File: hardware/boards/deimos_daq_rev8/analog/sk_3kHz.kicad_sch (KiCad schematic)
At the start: 9 parts, among them Q33001 MMBFJ113, Q33002 MMBFJ113, U33001 OPA196xDBV

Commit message: finish routing new encoder channels. spread nc channels on connectors and update enclosure graphics. only support 2-wire 4-20mA to protect ground.
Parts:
- renumbered C33001 to C45001, C33002 to C45002, C33003 to C45003, C33004 to C45004, Q33001 to Q45001, Q33002 to Q45002, R33001 to R45001, R33002 to R45002, U33001 to U45001
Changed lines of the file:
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@@
 		(on_board yes)
 		(dnp no)
-		(property "Reference" "#PWR286"
+		(property "Reference" "#PWR351"
 			(at 113.03 88.9 0)
 			(effects
@@
 		(on_board yes)
 		(dnp no)
-		(property "Reference" "C33001"
+		(property "Reference" "C45001"
 			(at 106.68 96.012 90)
 			(effects
@@
 		(on_board yes)
 		(dnp no)
-		(property "Reference" "#PWR283"
+		(property "Reference" "#PWR349"
 			(at 92.964 110.49 0)
 			(effects
@@
 		(on_board yes)
 		(dnp no)
-		(property "Reference" "R33001"
+		(property "Reference" "R45001"
 			(at 82.55 77.343 90)
 			(effects
@@
 		(on_board yes)
 		(dnp no)
-		(property "Reference" "#PWR278"
+		(property "Reference" "#PWR346"
 			(at 124.46 92.71 0)
 			(effects
@@
 		(on_board yes)
 		(dnp no)
-		(property "Reference" "Q33001"
+		(property "Reference" "Q45001"
 			(at 80.772 100.584 90)
 			(effects
@@
 		(on_board yes)
 		(dnp no)
-		(property "Reference" "#PWR280"
+		(property "Reference" "#PWR347"
 			(at 124.46 77.47 0)
 			(effects
@@
 		(on_board yes)
 		(dnp no)
-		(property "Reference" "Q33002"
+		(property "Reference" "Q45002"
 			(at 92.964 91.44 90)
 			(effects
@@
 		(on_board yes)
 		(dnp no)
-		(property "Reference" "U33001"
+		(property "Reference" "U45001"
 			(at 107.442 78.994 0)
 			(effects
@@
 		(on_board yes)
 		(dnp no)
-		(property "Reference" "R33002"
+		(property "Reference" "R45002"
 			(at 93.98 77.343 90)
 			(effects
@@
 		(on_board yes)
 		(dnp no)
-		(property "Reference" "C33003"
+		(property "Reference" "C45003"
 			(at 119.38 81.788 90)
 			(effects
@@
 		(on_board yes)
 		(dnp no)
-		(property "Reference" "C33004"
+		(property "Reference" "C45004"
 			(at 118.872 97.536 90)
 			(effects
@@
 		(on_board yes)
 		(dnp no)
-		(property "Reference" "C33002"
+		(property "Reference" "C45002"
 			(at 111.252 65.532 90)
 			(effects
@@
 		(on_board yes)
 		(dnp no)
-		(property "Reference" "#PWR281"
+		(property "Reference" "#PWR348"
 			(at 113.03 81.28 0)
 			(effects
@@
 		(on_board yes)
 		(dnp no)
-		(property "Reference" "#PWR200"
+		(property "Reference" "#PWR250"
 			(at 101.6 99.06 0)
 			(effects

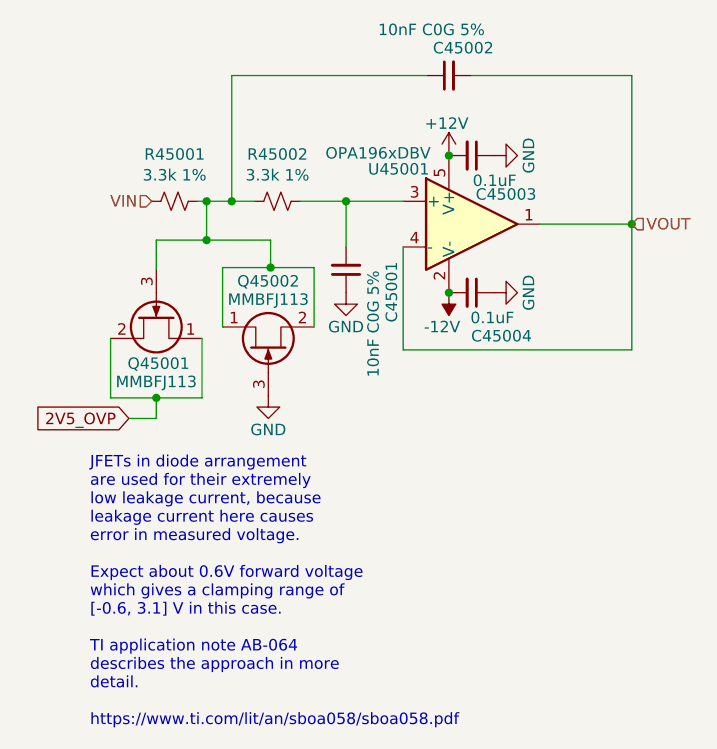
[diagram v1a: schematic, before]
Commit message: finish layout and generate fab files
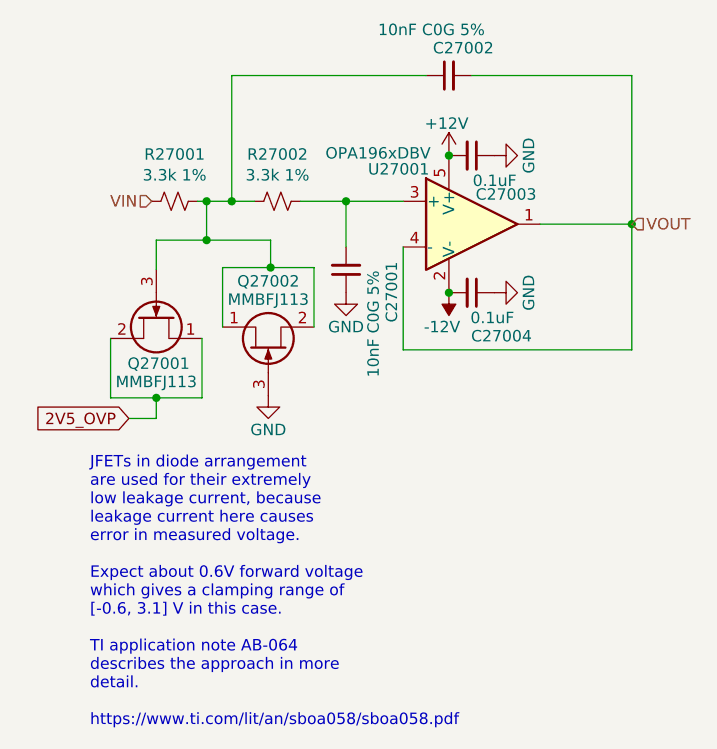
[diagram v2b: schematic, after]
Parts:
- renumbered C45001 to C27001, C45002 to C27002, C45003 to C27003, C45004 to C27004, Q45001 to Q27001, Q45002 to Q27002, R45001 to R27001, R45002 to R27002, U45001 to U27001
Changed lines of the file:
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@@
 		(on_board yes)
 		(dnp no)
-		(property "Reference" "#PWR351"
+		(property "Reference" "#PWR246"
 			(at 113.03 88.9 0)
 			(effects
@@
 		(on_board yes)
 		(dnp no)
-		(property "Reference" "C45001"
+		(property "Reference" "C27001"
 			(at 106.68 96.012 90)
 			(effects
@@
 		(on_board yes)
 		(dnp no)
-		(property "Reference" "#PWR349"
+		(property "Reference" "#PWR244"
 			(at 92.964 110.49 0)
 			(effects
@@
 		(on_board yes)
 		(dnp no)
-		(property "Reference" "R45001"
+		(property "Reference" "R27001"
 			(at 82.55 77.343 90)
 			(effects
@@
 		(on_board yes)
 		(dnp no)
-		(property "Reference" "#PWR346"
+		(property "Reference" "#PWR239"
 			(at 124.46 92.71 0)
 			(effects
@@
 		(on_board yes)
 		(dnp no)
-		(property "Reference" "Q45001"
+		(property "Reference" "Q27001"
 			(at 80.772 100.584 90)
 			(effects
@@
 		(on_board yes)
 		(dnp no)
-		(property "Reference" "#PWR347"
+		(property "Reference" "#PWR242"
 			(at 124.46 77.47 0)
 			(effects
@@
 		(on_board yes)
 		(dnp no)
-		(property "Reference" "Q45002"
+		(property "Reference" "Q27002"
 			(at 92.964 91.44 90)
 			(effects
@@
 		(on_board yes)
 		(dnp no)
-		(property "Reference" "U45001"
+		(property "Reference" "U27001"
 			(at 107.442 78.994 0)
 			(effects
@@
 		(on_board yes)
 		(dnp no)
-		(property "Reference" "R45002"
+		(property "Reference" "R27002"
 			(at 93.98 77.343 90)
 			(effects
@@
 		(on_board yes)
 		(dnp no)
-		(property "Reference" "C45003"
+		(property "Reference" "C27003"
 			(at 119.38 81.788 90)
 			(effects
@@
 		(on_board yes)
 		(dnp no)
-		(property "Reference" "C45004"
+		(property "Reference" "C27004"
 			(at 118.872 97.536 90)
 			(effects
@@
 		(on_board yes)
 		(dnp no)
-		(property "Reference" "C45002"
+		(property "Reference" "C27002"
 			(at 111.252 65.532 90)
 			(effects
@@
 		(on_board yes)
 		(dnp no)
-		(property "Reference" "#PWR348"
+		(property "Reference" "#PWR243"
 			(at 113.03 81.28 0)
 			(effects
@@
 		(on_board yes)
 		(dnp no)
-		(property "Reference" "#PWR250"
+		(property "Reference" "#PWR185"
 			(at 101.6 99.06 0)
 			(effects

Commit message: use better diode prot for digital I/O and dacs. generate fab files.
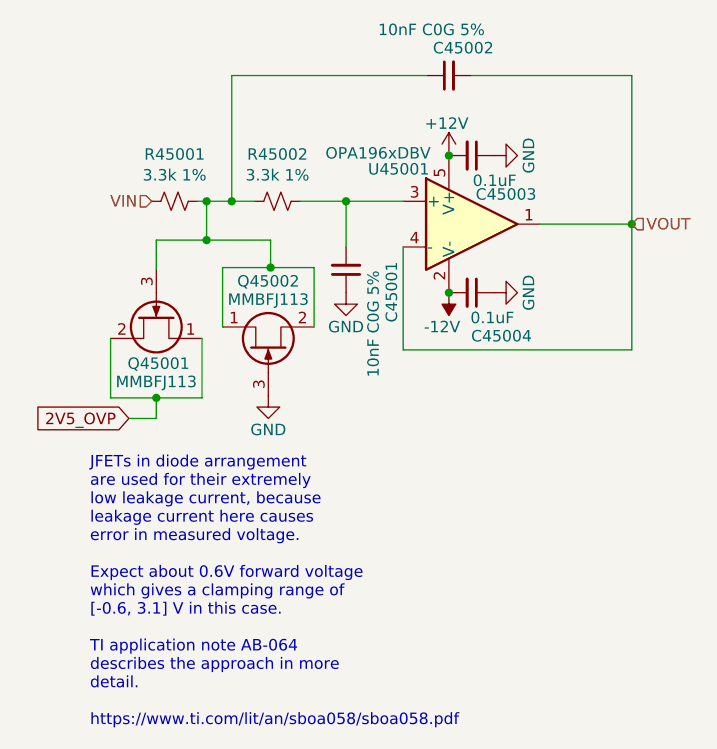
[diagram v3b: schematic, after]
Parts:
- renumbered C27001 to C45001, C27002 to C45002, C27003 to C45003, C27004 to C45004, Q27001 to Q45001, Q27002 to Q45002, R27001 to R45001, R27002 to R45002, U27001 to U45001
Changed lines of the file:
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@@
 		(on_board yes)
 		(dnp no)
-		(property "Reference" "#PWR246"
+		(property "Reference" "#PWR351"
 			(at 113.03 88.9 0)
 			(effects
@@
 		(on_board yes)
 		(dnp no)
-		(property "Reference" "C27001"
+		(property "Reference" "C45001"
 			(at 106.68 96.012 90)
 			(effects
@@
 		(on_board yes)
 		(dnp no)
-		(property "Reference" "#PWR244"
+		(property "Reference" "#PWR349"
 			(at 92.964 110.49 0)
 			(effects
@@
 		(on_board yes)
 		(dnp no)
-		(property "Reference" "R27001"
+		(property "Reference" "R45001"
 			(at 82.55 77.343 90)
 			(effects
@@
 		(on_board yes)
 		(dnp no)
-		(property "Reference" "#PWR239"
+		(property "Reference" "#PWR346"
 			(at 124.46 92.71 0)
 			(effects
@@
 		(on_board yes)
 		(dnp no)
-		(property "Reference" "Q27001"
+		(property "Reference" "Q45001"
 			(at 80.772 100.584 90)
 			(effects
@@
 		(on_board yes)
 		(dnp no)
-		(property "Reference" "#PWR242"
+		(property "Reference" "#PWR347"
 			(at 124.46 77.47 0)
 			(effects
@@
 		(on_board yes)
 		(dnp no)
-		(property "Reference" "Q27002"
+		(property "Reference" "Q45002"
 			(at 92.964 91.44 90)
 			(effects
@@
 		(on_board yes)
 		(dnp no)
-		(property "Reference" "U27001"
+		(property "Reference" "U45001"
 			(at 107.442 78.994 0)
 			(effects
@@
 		(on_board yes)
 		(dnp no)
-		(property "Reference" "R27002"
+		(property "Reference" "R45002"
 			(at 93.98 77.343 90)
 			(effects
@@
 		(on_board yes)
 		(dnp no)
-		(property "Reference" "C27003"
+		(property "Reference" "C45003"
 			(at 119.38 81.788 90)
 			(effects
@@
 		(on_board yes)
 		(dnp no)
-		(property "Reference" "C27004"
+		(property "Reference" "C45004"
 			(at 118.872 97.536 90)
 			(effects
@@
 		(on_board yes)
 		(dnp no)
-		(property "Reference" "C27002"
+		(property "Reference" "C45002"
 			(at 111.252 65.532 90)
 			(effects
@@
 		(on_board yes)
 		(dnp no)
-		(property "Reference" "#PWR243"
+		(property "Reference" "#PWR348"
 			(at 113.03 81.28 0)
 			(effects
@@
 		(on_board yes)
 		(dnp no)
-		(property "Reference" "#PWR185"
+		(property "Reference" "#PWR250"
 			(at 101.6 99.06 0)
 			(effects
